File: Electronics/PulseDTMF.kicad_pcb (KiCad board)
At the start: 2 copper layers, 13 parts, among them P1 CONN_01X04, P2 CONN_01X04, U1 MSP430G2230ID, U2 LD1117S33TR

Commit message: New board.
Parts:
- added C6: 100nF, Capacitors_SMD:C_0805_HandSoldering, F.Cu at (240.0, 128.9)
- added R3: 1K, Resistors_SMD:R_0805_HandSoldering, F.Cu at (237.5, 128.9)
- C2, C3, C4, C5: moved to B.Cu
- D2: value DIODE -> D; footprint Diodes_SMD:Diode-SMA_Handsoldering -> Diodes_SMD:SMA_Standard; moved to B.Cu
- U2: footprint SMD_Packages:SOT-223 -> TO_SOT_Packages_SMD:SOT-223; moved to B.Cu
- moved P1 112.0 mm to (256.5, 134.6), turned to 270 degrees
- moved D1 111.9 mm to (257.8, 128.9), turned to 270 degrees
- moved R2 109.4 mm to (255.3, 128.9), turned to 270 degrees
- moved U2 107.6 mm to (253.4, 128.9), turned to 90 degrees
- moved U1 104.0 mm to (249.6, 129.5), turned to 180 degrees
- moved C5 101.4 mm to (247.0, 128.9), turned to 270 degrees
- moved C4 98.9 mm to (244.5, 128.9), turned to 270 degrees
- moved R1 97.1 mm to (242.6, 128.9), turned to 90 degrees
- moved C3 96.4 mm to (241.9, 128.9), turned to 270 degrees
- moved C2 94.0 mm to (239.4, 128.9), turned to 270 degrees
- moved P2 92.6 mm to (236.2, 134.6), turned to 90 degrees
- moved D2 90.9 mm to (236.2, 128.9), turned to 270 degrees
- moved C1 89.7 mm to (234.9, 128.9), turned to 90 degrees
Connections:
- D2 pad 1: /LINE -> Net-(C2-Pad1)
- D2 pad 2: Net-(C2-Pad1) -> /LINE
- U1 pad 2: /SIGNAL -> /DIAL1
- U1 pad 4: /DIAL1 -> /SIGNAL
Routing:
- net VDD: track 0.00 -> 21.9 mm
- net /DIAL1: track 0.00 -> 21.8 mm
- net Net-(C2-Pad1): track 0.00 -> 16.1 mm
- net /DIAL2: track 0.00 -> 12.5 mm
- net /SIGNAL: track 0.00 -> 11.8 mm
- net /SBWTDIO: track 0.00 -> 11.3 mm
- net /SBWTCK: track 0.00 -> 8.99 mm
- net Net-(C1-Pad2): track 0.00 -> 8.81 mm
- net /LINE: track 0.00 -> 8.71 mm
- net /LED: track 0.00 -> 3.57 mm
- net Net-(D1-Pad1): track 0.00 -> 2.66 mm
- added copper zone on B.Cu, net GND
- added copper zone on F.Cu, net GND
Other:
- board outline added: 25.4 x 12.7 mm
- net class Default: trace_width 0.254 -> 0.508
- net class Minimal added: clearance 0.1524, trace_width 0.1524, via_dia 0.6858, via_drill 0.3302
- net class Power added: clearance 0.254, trace_width 1.016, via_dia 0.889, via_drill 0.635
- rule trace_min: 0.254 -> 0.1524
- rule via_min_drill: 0.508 -> 0.3302
- rule via_min_size: 0.889 -> 0.6858

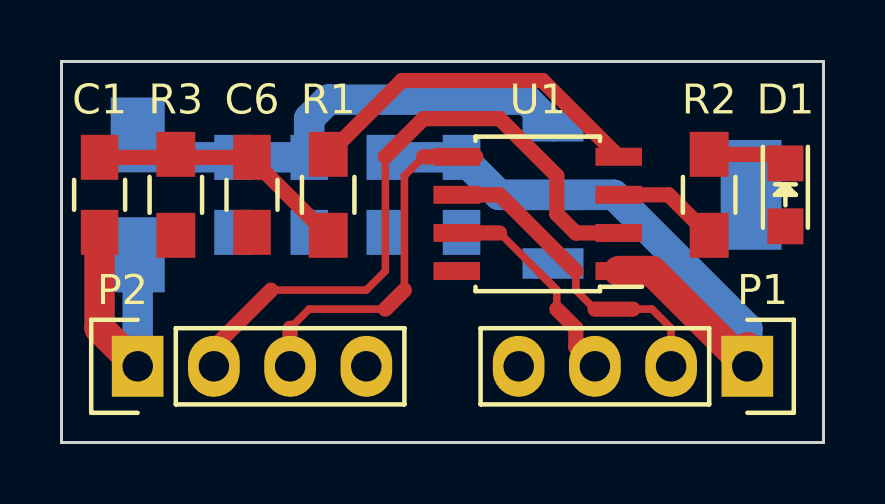
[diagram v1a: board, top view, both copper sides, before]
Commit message: Changed PCB version with 25 thou signal traces, correct component references and correctly named GERBER files.
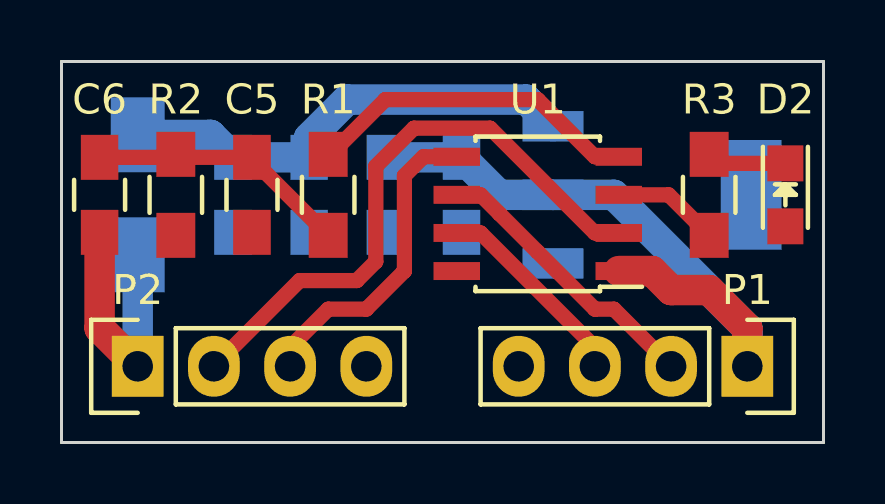
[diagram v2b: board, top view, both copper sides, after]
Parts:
- C1: moved to B.Cu
- C2, C4: value 1uF -> 100nF
- C3, C6: value 100nF -> 1uF
- C5: moved to F.Cu
- D1: value LED -> D; footprint LEDs:LED-0805 -> Diodes_SMD:SMA_Standard; moved to B.Cu
- D2: value D -> LED; footprint Diodes_SMD:SMA_Standard -> LEDs:LED-0805; moved to F.Cu
- moved D1 21.6 mm to (236.2, 128.9)
- moved D2 21.6 mm to (257.8, 128.9)
- moved R2 17.8 mm to (237.5, 128.9), turned to 90 degrees
- moved R3 17.8 mm to (255.3, 128.9), turned to 270 degrees
- moved C5 6.98 mm to (240.0, 128.9), turned to 90 degrees
- moved C6 5.08 mm to (234.9, 128.9)
- moved C1 4.45 mm to (239.4, 128.9), turned to 270 degrees
- moved C2 2.54 mm to (241.9, 128.9)
- moved C3 2.54 mm to (244.5, 128.9)
- moved C4 2.54 mm to (247.0, 128.9)
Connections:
- C1 pad 1: /LINE -> Net-(C1-Pad1)
- C1 pad 2: Net-(C1-Pad2) -> GND
- C2 pad 1: Net-(C2-Pad1) -> Net-(C1-Pad1)
- C3 pad 1: Net-(C2-Pad1) -> VDD
- C5 pad 1: VDD -> GND
- C5 pad 2: GND -> Net-(C5-Pad2)
- C6 pad 1: GND -> /LINE
- C6 pad 2: Net-(C1-Pad2) -> Net-(C5-Pad2)
- D1 pad 1: Net-(D1-Pad1) -> Net-(C1-Pad1)
- D1 pad 2: GND -> /LINE
- D2 pad 1: Net-(C2-Pad1) -> Net-(D2-Pad1)
- D2 pad 2: /LINE -> GND
- R1 pad 1: Net-(C1-Pad2) -> Net-(C5-Pad2)
- R2 pad 1: Net-(D1-Pad1) -> GND
- R2 pad 2: /LED -> Net-(C5-Pad2)
- R3 pad 1: GND -> Net-(D2-Pad1)
- R3 pad 2: Net-(C1-Pad2) -> /LED
- U2 pad 3: Net-(C2-Pad1) -> Net-(C1-Pad1)
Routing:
- net Net-(C2-Pad1): track 16.1 -> 0.00 mm
- net Net-(C1-Pad1): track 0.00 -> 15.7 mm
- net Net-(C1-Pad2): track 8.81 -> 0.00 mm
- net Net-(C5-Pad2): track 0.00 -> 8.61 mm
- net Net-(D2-Pad1): track 0.00 -> 3.09 mm
- net Net-(D1-Pad1): track 2.66 -> 0.00 mm
- net /SBWTCK: track 8.99 -> 6.82 mm
- net /DIAL2: track 12.5 -> 10.7 mm
- net /DIAL1: track 21.8 -> 20.1 mm
- net /SBWTDIO: track 11.3 -> 10.1 mm
- net /SIGNAL: track 11.8 -> 11.2 mm
